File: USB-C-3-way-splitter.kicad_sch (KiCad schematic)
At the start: 33 parts, among them J1 USB_C_Receptacle_USB2.0, J2 Conn_01x05_Socket, J3 Conn_01x05_Socket, J4 Conn_01x05_Socket, U1 LM393, U2 SiP32509

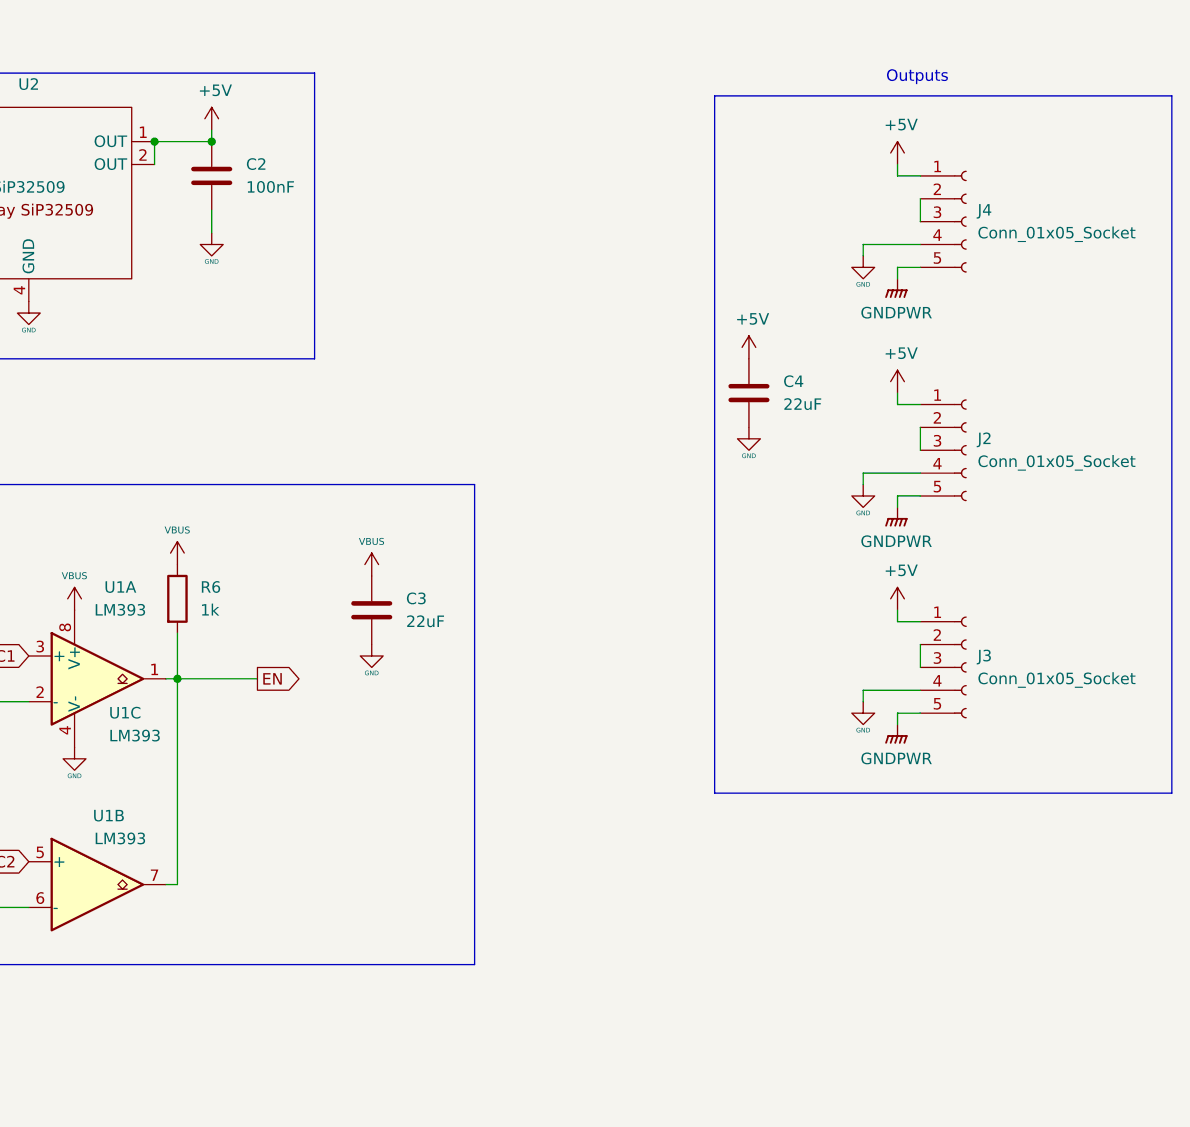
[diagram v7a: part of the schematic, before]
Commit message: Redesigned to fix circuit design error
The previous revision had the comparator outputs implemented as an AND instead of an OR, which was preventing the switch from ever turning on.
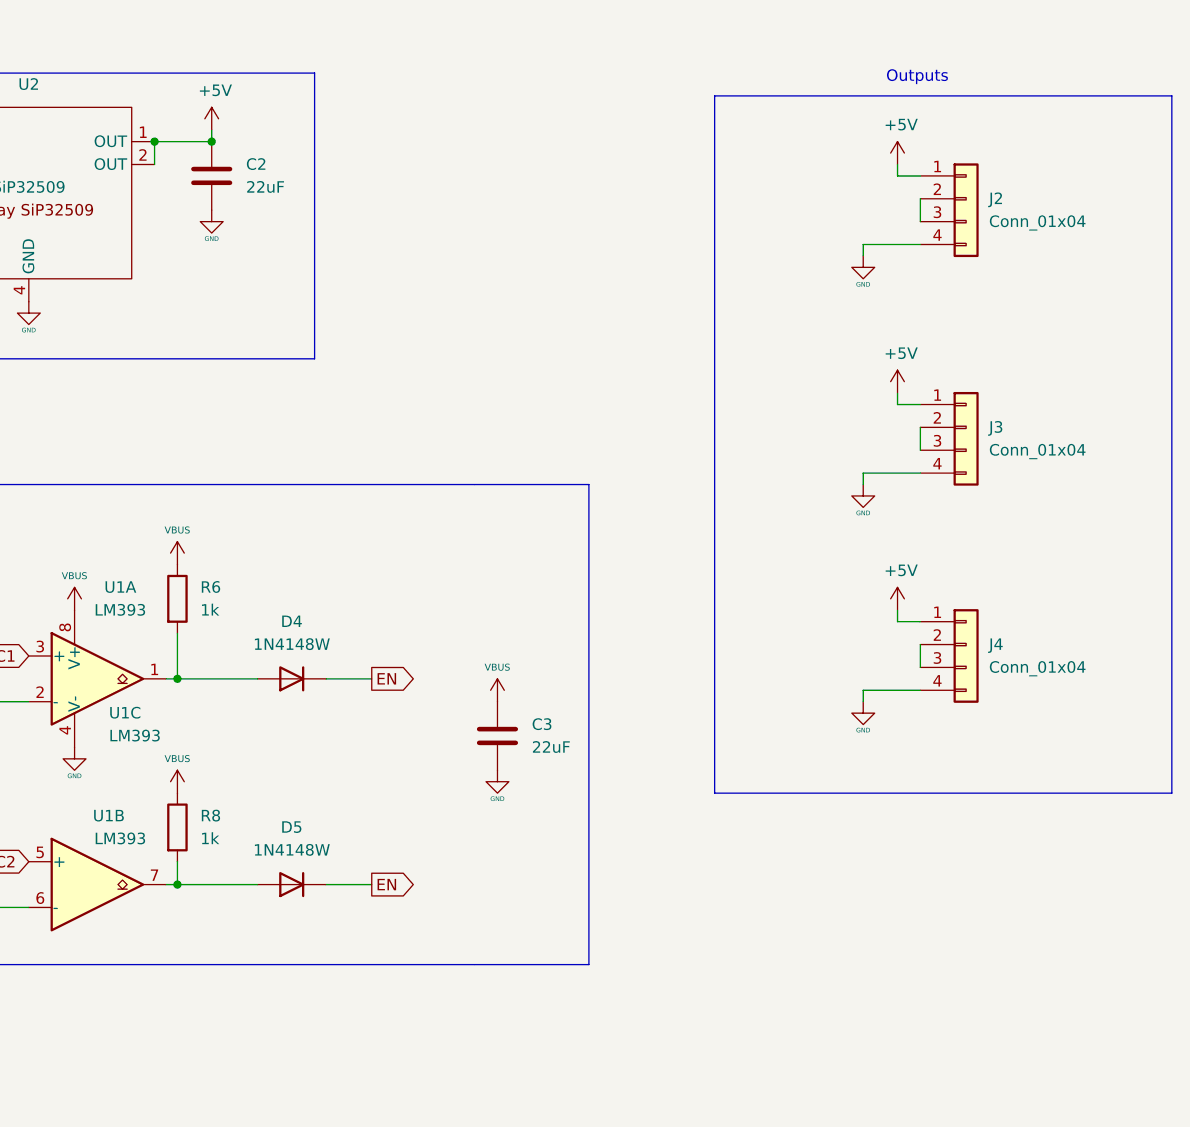
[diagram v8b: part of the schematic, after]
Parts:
- removed C2: 100nF, Capacitor_SMD:C_0805_2012Metric_Pad1.18x1.45mm_HandSolder, symbol Device:C
- removed J2, J3, J4: Conn_01x05_Socket, Connector_PinHeader_2.00mm:PinHeader_1x05_P2.00mm_Vertical, symbol Connector:Conn_01x05_Socket
- added D4, D5: 1N4148W, Diode_SMD:D_SOD-123, symbol Diode:1N4148W
- added J2, J3, J4: Conn_01x04, Connector_PinHeader_2.00mm:PinHeader_1x04_P2.00mm_Vertical, symbol Connector_Generic:Conn_01x04
- added R8: 1k, Resistor_SMD:R_0805_2012Metric_Pad1.20x1.40mm_HandSolder, symbol Device:R
- renumbered C4 to C2
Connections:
- net +5V: now also J2.1 (Pin_1), J3.1 (Pin_1), J4.1 (Pin_1)
- net EN: now also D4.1 (K), D5.1 (K); no longer R6.2, U1.1, U1.7
- net GND: now also J2.4 (Pin_4), J3.4 (Pin_4), J4.4 (Pin_4)
- net VBUS: now also R8.1
- new net: D4.2 (A), R6.2, U1.1
- new net: D5.2 (A), R8.2, U1.7
- new net: J2.2 (Pin_2), J2.3 (Pin_3)
- new net: J3.2 (Pin_2), J3.3 (Pin_3)
- new net: J4.2 (Pin_2), J4.3 (Pin_3)
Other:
- moved on the sheet: C2, C3
